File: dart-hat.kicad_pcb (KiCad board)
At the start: 4 copper layers, 114 x 65 mm, 127 parts, among them IC1 PCA9615DPJ, J1 XT60 Female, J2 Raspberry_Pi_2_3, J3 CAN_CON, J4 SM07B-SRSS-TBLFSN, M1 Motor_Servo, M2 Motor_Servo, M3 Motor_Servo, M4 Motor_Servo, Q1 SI7611DN-T1-GE3, Q2 SI7611DN-T1-GE3, Q3 DMMT5401, Q4 Q_NMOS_SGD, U1 CAT24C32YI-GT3, U2 MCP2515-xSO, U3 MCP2562-H-P, U4 BMI088, U5 PCA9685PW, U6 IFX27001TFV, U7 LM25088MH-2, Y1 16MHz

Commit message: ordered
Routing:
- net GND: vias 454 -> 488
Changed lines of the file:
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@@
     (thickness 1.6)
     (drawings 1056)
-    (tracks 1499)
+    (tracks 1533)
     (zones 0)
     (modules 127)
@@
   )
   (setup
-    (last_trace_width 0.6)
+    (last_trace_width 0.25)
     (user_trace_width 0.05)
     (user_trace_width 0.1)
@@
     (visible_elements 7FFFFFFF)
     (pcbplotparams
-      (layerselection 0x00030_ffffffff)
-      (usegerberextensions false)
+      (layerselection 0x010fc_ffffffff)
+      (usegerberextensions true)
       (usegerberattributes false)
       (usegerberadvancedattributes false)
       (creategerberjobfile false)
       (excludeedgelayer true)
-      (linewidth 0.100000)
+      (linewidth 0.150000)
       (plotframeref false)
       (viasonmask false)
@@
       (padsonsilk false)
       (subtractmaskfromsilk false)
-      (outputformat 4)
+      (outputformat 1)
       (mirror false)
       (drillshape 0)
@@
     (tags "LED handsolder")
     (attr smd)
-    (fp_text reference D5 (at -2.89412 2.03) (layer B.SilkS)
+    (fp_text reference D5 (at -3.11212 0.054) (layer B.SilkS)
       (effects (font (size 1 1) (thickness 0.15)) (justify mirror))
     )
@@
     (tags "resistor handsolder")
     (attr smd)
-    (fp_text reference R18 (at 3.475 1.65) (layer B.SilkS)
+    (fp_text reference R18 (at 3.475 -0.11684) (layer B.SilkS)
       (effects (font (size 1 1) (thickness 0.15)) (justify mirror))
     )
@@
   (via (at 141.478 65.278) (size 0.6) (drill 0.4) (layers F.Cu B.Cu) (net 1))
   (via (at 140.462 65.278) (size 0.6) (drill 0.4) (layers F.Cu B.Cu) (net 1))
+  (via (at 215.138 105.156) (size 0.6) (drill 0.4) (layers F.Cu B.Cu) (net 1))
+  (via (at 215.138 104.14) (size 0.6) (drill 0.4) (layers F.Cu B.Cu) (net 1))
+  (via (at 215.138 103.124) (size 0.6) (drill 0.4) (layers F.Cu B.Cu) (net 1))
+  (via (at 215.138 102.108) (size 0.6) (drill 0.4) (layers F.Cu B.Cu) (net 1))
+  (via (at 214.376 102.616) (size 0.6) (drill 0.4) (layers F.Cu B.Cu) (net 1))
+  (via (at 214.376 103.632) (size 0.6) (drill 0.4) (layers F.Cu B.Cu) (net 1))
+  (via (at 214.376 104.648) (size 0.6) (drill 0.4) (layers F.Cu B.Cu) (net 1))
+  (via (at 215.9 95.758) (size 0.6) (drill 0.4) (layers F.Cu B.Cu) (net 1))
+  (via (at 215.138 94.996) (size 0.6) (drill 0.4) (layers F.Cu B.Cu) (net 1))
+  (via (at 192.532 100.838) (size 0.6) (drill 0.4) (layers F.Cu B.Cu) (net 1))
+  (via (at 191.516 100.838) (size 0.6) (drill 0.4) (layers F.Cu B.Cu) (net 1))
+  (via (at 190.5 100.838) (size 0.6) (drill 0.4) (layers F.Cu B.Cu) (net 1))
+  (via (at 189.484 100.838) (size 0.6) (drill 0.4) (layers F.Cu B.Cu) (net 1))
+  (via (at 188.468 100.838) (size 0.6) (drill 0.4) (layers F.Cu B.Cu) (net 1))
+  (via (at 187.452 100.838) (size 0.6) (drill 0.4) (layers F.Cu B.Cu) (net 1))
+  (via (at 186.182 100.838) (size 0.6) (drill 0.4) (layers F.Cu B.Cu) (net 1))
+  (via (at 186.182 102.108) (size 0.6) (drill 0.4) (layers F.Cu B.Cu) (net 1))
+  (via (at 187.452 102.108) (size 0.6) (drill 0.4) (layers F.Cu B.Cu) (net 1))
+  (via (at 188.468 102.108) (size 0.6) (drill 0.4) (layers F.Cu B.Cu) (net 1))
+  (via (at 189.484 102.108) (size 0.6) (drill 0.4) (layers F.Cu B.Cu) (net 1))
+  (via (at 190.5 102.108) (size 0.6) (drill 0.4) (layers F.Cu B.Cu) (net 1))
+  (via (at 191.516 102.108) (size 0.6) (drill 0.4) (layers F.Cu B.Cu) (net 1))
+  (via (at 192.532 102.108) (size 0.6) (drill 0.4) (layers F.Cu B.Cu) (net 1))
+  (via (at 174.752 77.216) (size 0.6) (drill 0.4) (layers F.Cu B.Cu) (net 1))
+  (via (at 175.514 76.708) (size 0.6) (drill 0.4) (layers F.Cu B.Cu) (net 1))
+  (via (at 176.276 76.2) (size 0.6) (drill 0.4) (layers F.Cu B.Cu) (net 1))
+  (via (at 177.038 75.692) (size 0.6) (drill 0.4) (layers F.Cu B.Cu) (net 1))
+  (via (at 177.8 75.184) (size 0.6) (drill 0.4) (layers F.Cu B.Cu) (net 1))
+  (via (at 178.562 74.676) (size 0.6) (drill 0.4) (layers F.Cu B.Cu) (net 1))
+  (via (at 199.898 59.436) (size 0.6) (drill 0.4) (layers F.Cu B.Cu) (net 1))
+  (via (at 200.66 58.674) (size 0.6) (drill 0.4) (layers F.Cu B.Cu) (net 1))
+  (via (at 201.422 59.436) (size 0.6) (drill 0.4) (layers F.Cu B.Cu) (net 1))
+  (via (at 202.184 58.674) (size 0.6) (drill 0.4) (layers F.Cu B.Cu) (net 1))
+  (via (at 202.184 60.198) (size 0.6) (drill 0.4) (layers F.Cu B.Cu) (net 1))
   (segment (start 205.102 85.275) (end 205.127 85.3) (width 0.2) (layer B.Cu) (net 2))
   (segment (start 205.102 83.3) (end 205.102 85.275) (width 0.2) (layer B.Cu) (net 2))

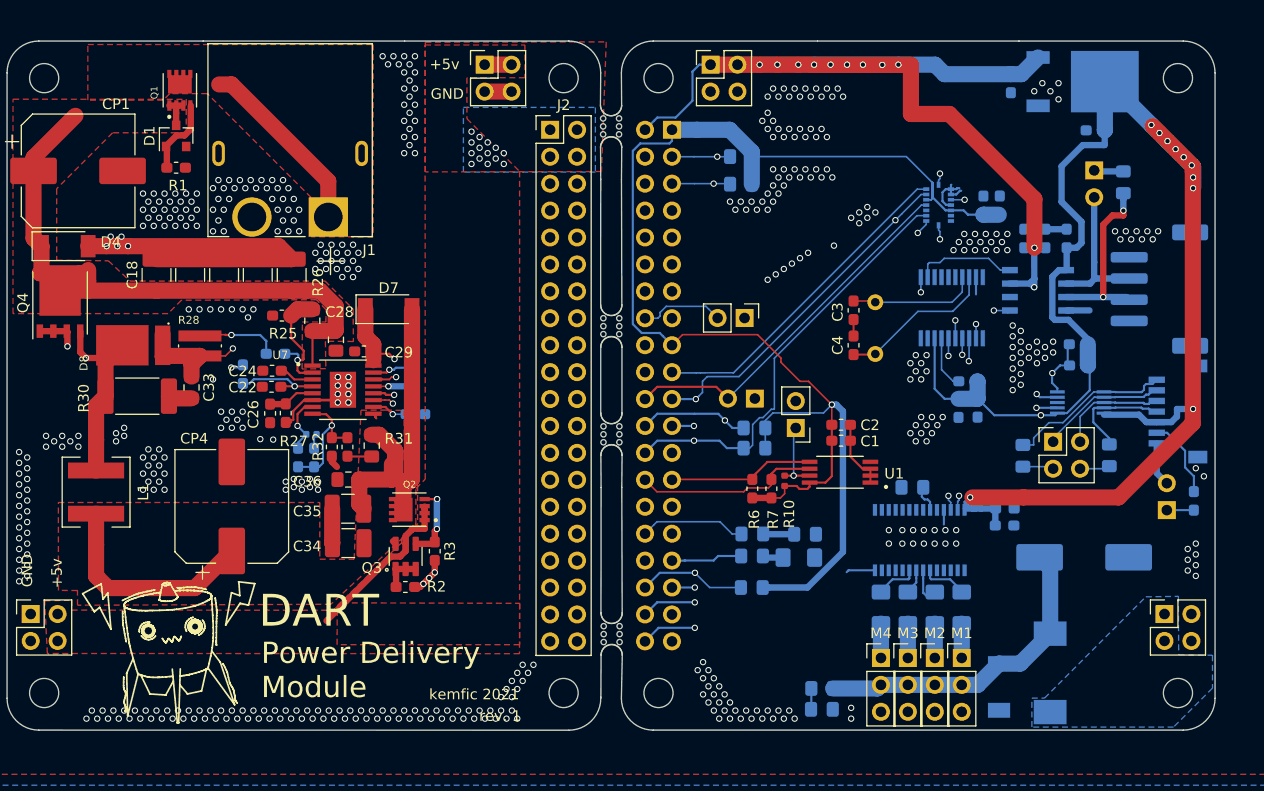
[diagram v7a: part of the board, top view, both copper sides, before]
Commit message: [rev.2 fixes]  - fix Q4 net pin assignment  - removed UVLO  - fix kelvin connection on R_sense  - fix MCP2515 symbol + pinout  - changed oscillator capacitors for 18uF load capacitance  - PCA9615 biasing resistors
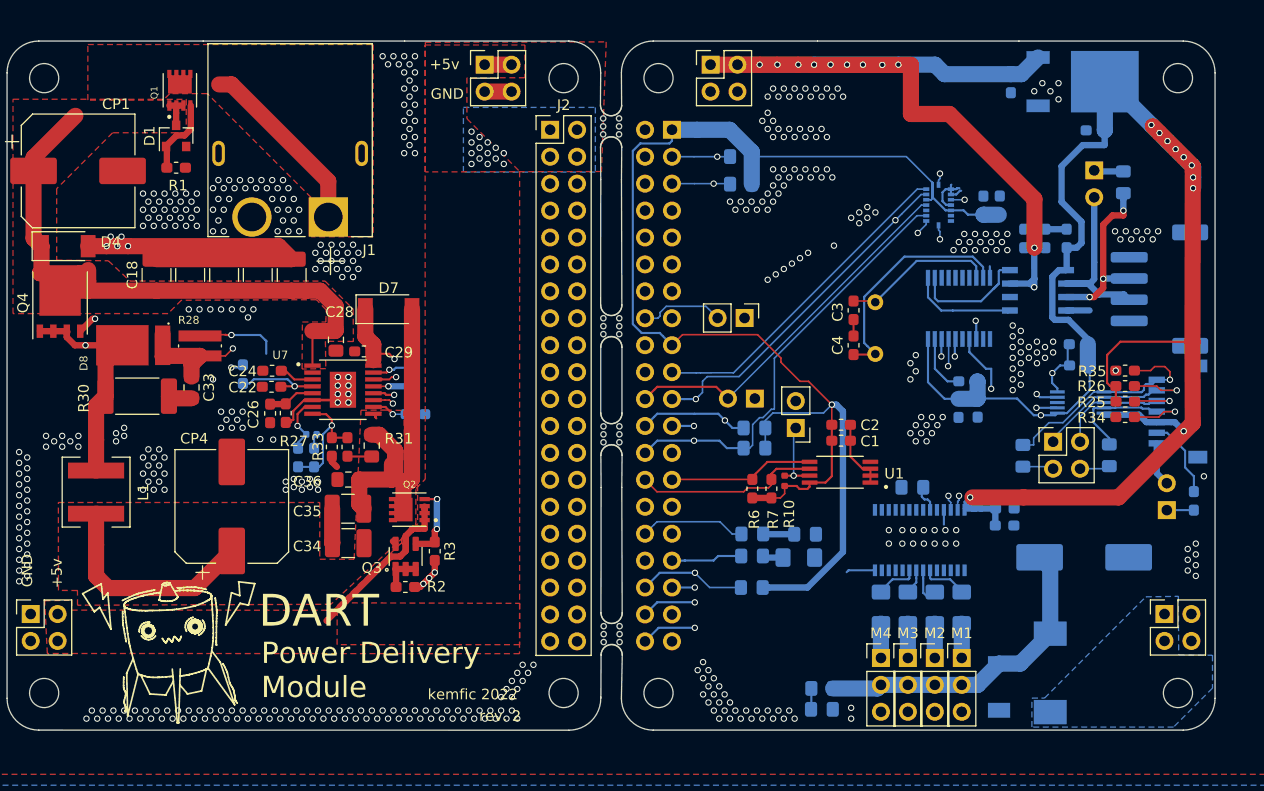
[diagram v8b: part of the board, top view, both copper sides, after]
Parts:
- removed C25: NU, Capacitor_SMD:C_0603_1608Metric_Pad1.05x0.95mm_HandSolder
- added R34: 390, Resistor_SMD:R_0603_1608Metric_Pad1.05x0.95mm_HandSolder, F.Cu at (208.5, 90.2)
- added R35: 390, Resistor_SMD:R_0603_1608Metric_Pad1.05x0.95mm_HandSolder, F.Cu at (208.5, 85.8)
- C3, C4: value 22pF -> 36pF
- JP1: value WP_EN -> Jumper_NO_Small
- JP3: value CAN_INT -> Jumper
- JP7: value BMI_INT -> Jumper_NO_Small
- R25: value 2.36k -> 390
- R26: value 54.9k -> 390; footprint Resistor_SMD:R_0805_2012Metric_Pad1.15x1.40mm_HandSolder -> Resistor_SMD:R_0603_1608Metric_Pad1.05x0.95mm_HandSolder
- U2: value MCP2515-xSO -> MCP2515-xST
- moved R25 80.0 mm to (208.5, 88.7), turned to 0 degrees
- moved R26 76.9 mm to (208.5, 87.2), turned to 0 degrees
- moved U2 0.67 mm to (192.8, 79.9)
- renumbered T_CAN to JP2, SHD to JP5
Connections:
- J3 pad 1: GND -> (no net)
- J3 pad 2: /Can Interface/CAN_L -> /Can Interface/CAN_H
- J3 pad 3: /Can Interface/CAN_H -> /Can Interface/CAN_L
- J3 pad 4: Net-(J3-Pad4) -> GND
- Q4 pad 1: Net-(Q4-Pad2) -> Net-(C30-Pad1)
- R25 pad 1: Net-(C25-Pad1) -> +3V3
- R25 pad 2: GND -> /differential i2c iface/SDA+
- R26 pad 1: +BATT -> +3V3
- R26 pad 2: Net-(C25-Pad1) -> /differential i2c iface/SCL+
- U2 pad 10: Net-(U2-Pad10) -> GND
- U2 pad 12: Net-(JP3-Pad1) -> Net-(U2-Pad12)
- U2 pad 13: /MISO_CAN -> Net-(JP3-Pad1)
- U2 pad 14: /MOSI_CAN -> /SCLK_CAN
- U2 pad 15: /SCLK_CAN -> Net-(U2-Pad15)
- U2 pad 16: /CS_CAN -> /MOSI_CAN
- U2 pad 17: Net-(R15-Pad2) -> /MISO_CAN
- U2 pad 18: +3V3 -> /CS_CAN
- U2 pad 19: (no net) -> Net-(R15-Pad2)
- U2 pad 20: (no net) -> +3V3
- U2 pad 7: Net-(C3-Pad1) -> Net-(U2-Pad7)
- U2 pad 8: Net-(C4-Pad2) -> Net-(C3-Pad1)
- U2 pad 9: GND -> Net-(C4-Pad2)
- U7 pad 2: Net-(C25-Pad1) -> Net-(U7-Pad2)
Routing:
- net +3V3: track 153.9 -> 166.2 mm
- net Net-(C25-Pad1): track 11.8 -> 0.00 mm, vias 1 -> 0
- net +5V: track 150.2 -> 139.9 mm
- net Net-(C4-Pad2): track 14.9 -> 22.1 mm
- net Net-(Q4-Pad2): track 55.8 -> 48.7 mm
- net /MISO_CAN: track 48.9 -> 42.0 mm
- net /SCLK_CAN: track 61.5 -> 55.3 mm
- net /differential i2c iface/SCL+: track 12.0 -> 18.0 mm, vias 0 -> 1
- net /differential i2c iface/SDA-: track 10.4 -> 16.3 mm, vias 0 -> 1
- net /differential i2c iface/SCL-: track 15.8 -> 21.5 mm, vias 0 -> 1
- net Net-(C30-Pad1): track 74.1 -> 79.1 mm
- net /differential i2c iface/SDA+: track 10.3 -> 14.8 mm, vias 0 -> 1
- net /Can Interface/CAN_L: track 13.9 -> 17.1 mm
- net Net-(U2-Pad2): track 10.1 -> 12.9 mm
- net Net-(C3-Pad1): track 12.1 -> 14.5 mm
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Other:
- board text added: "@kemfic 2022"
- board text added: "CANH CANL GND"
- board text added: "kemfic 2022"
- board text added: "rev. 2"
- board text removed: "@kemfic 2021"
- board text removed: "GND CANL CANH"
- board text removed: "kemfic 2021"
- board text removed: "rev. 1"
